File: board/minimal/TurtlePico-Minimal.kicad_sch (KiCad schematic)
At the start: 25 parts, among them J1 USB_C_Receptacle_USB2.0_14P, Q1 PMOS, Q2 PMOS, SW1 SW_Push, U1 RP2040, U2 STUSB4500QTR, U3 AP63203WU

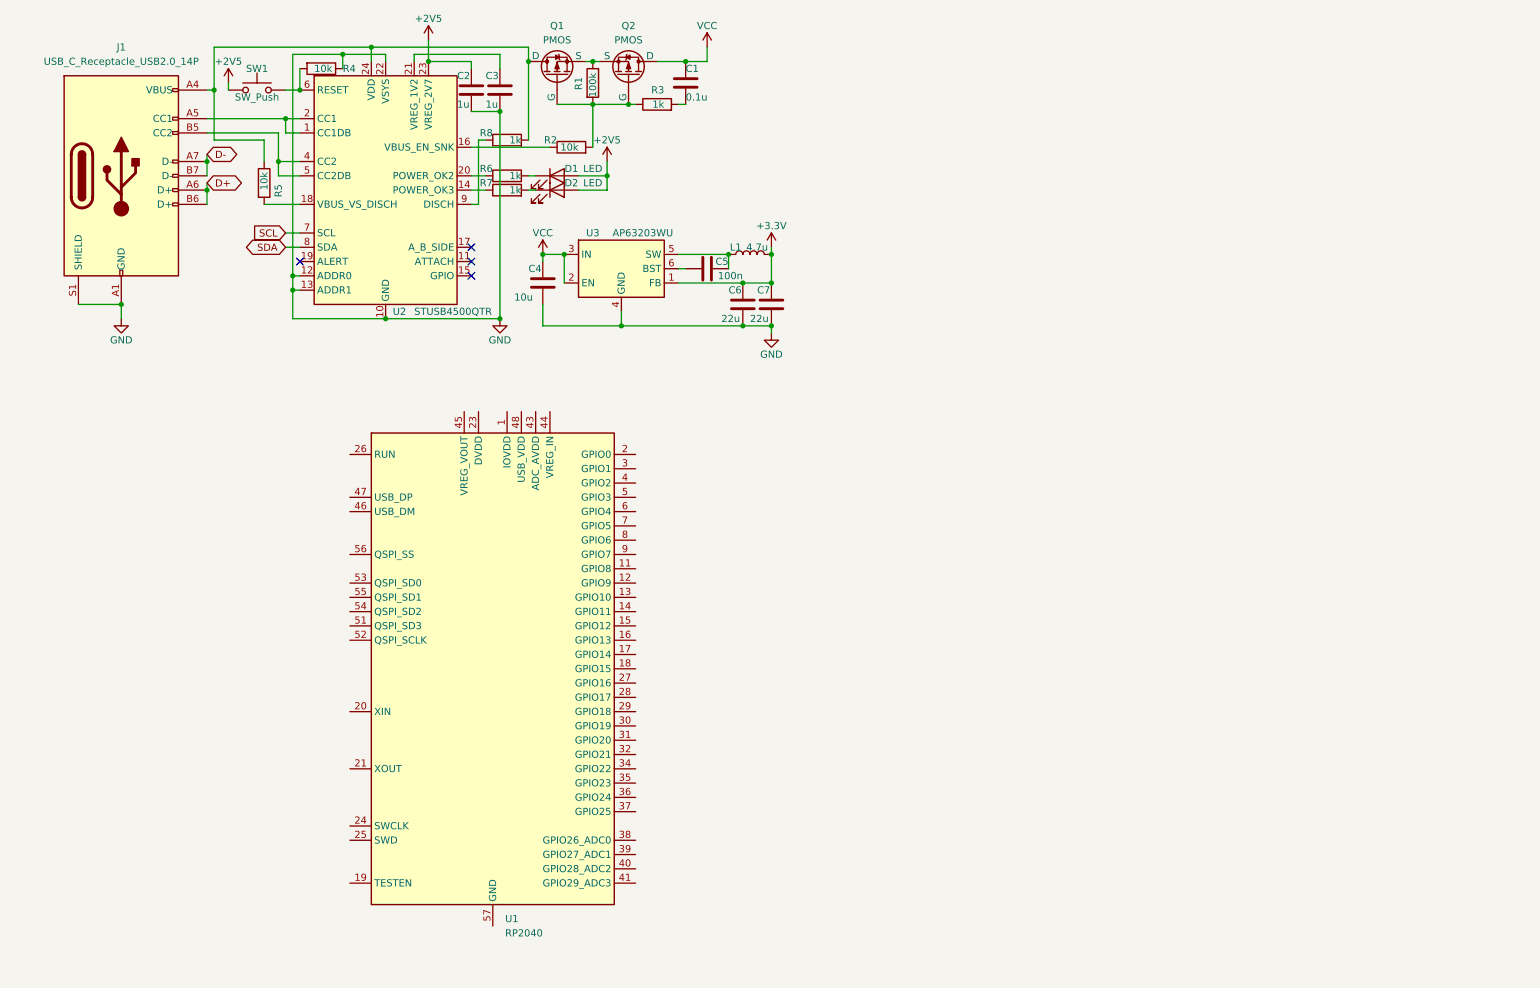
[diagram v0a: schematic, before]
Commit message: update minimal model
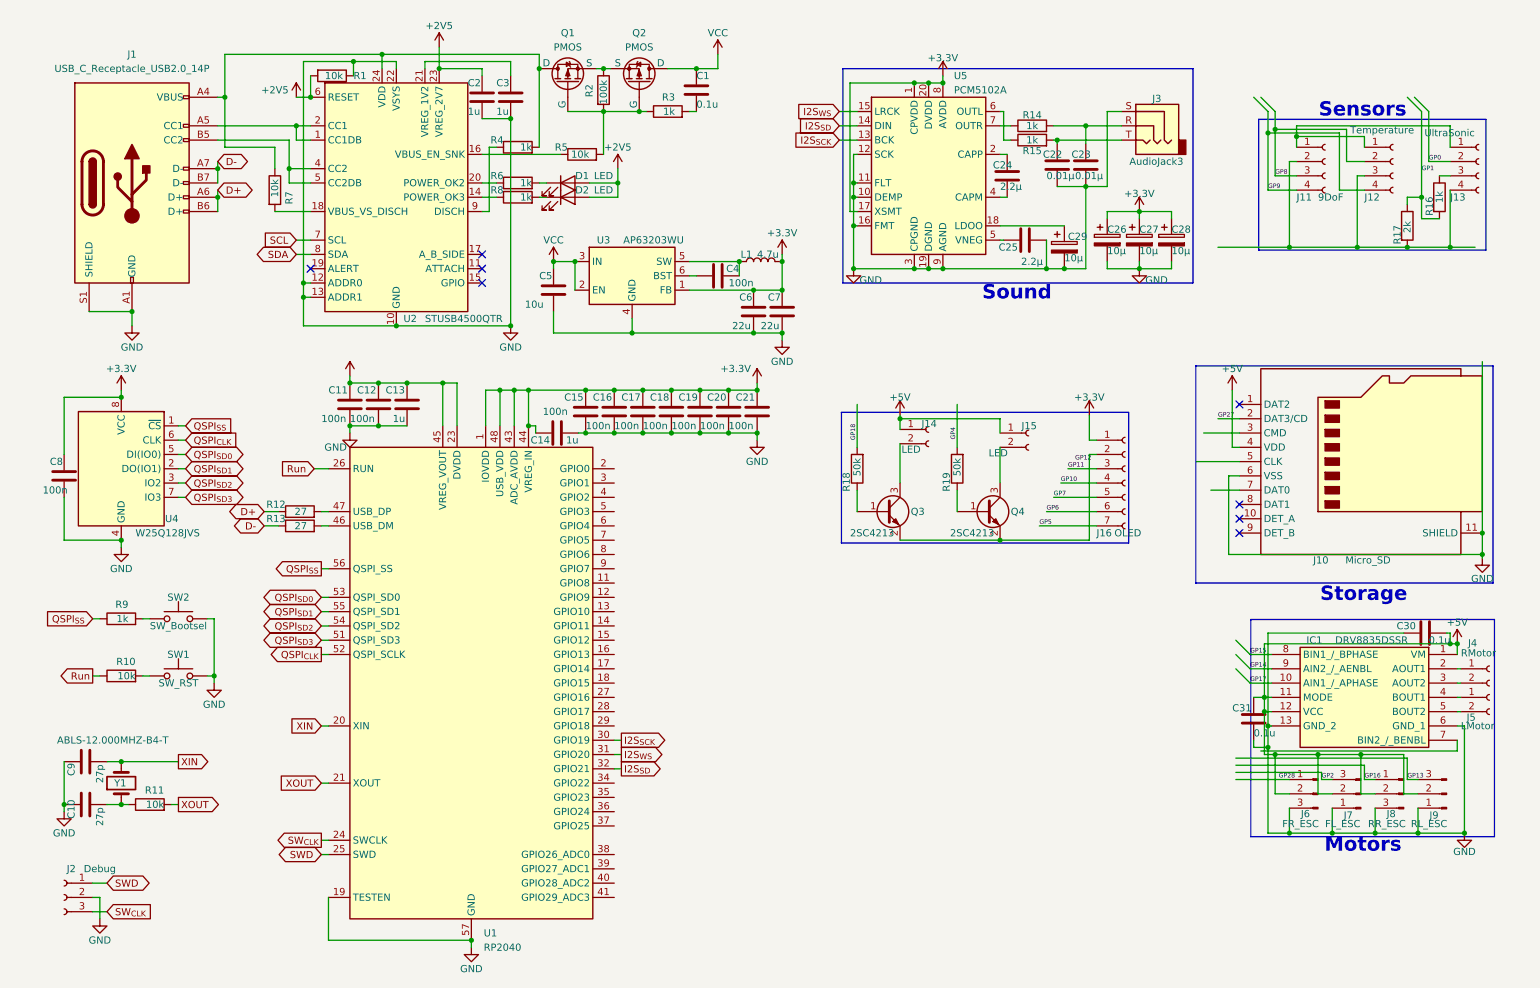
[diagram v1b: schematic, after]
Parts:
- added C10, C9: 27p, symbol Device:C
- added C11, C12, C15, C16, C17, C18, C19, C20, C21, C8: 100n, symbol Device:C
- added C13, C14: 1u, symbol Device:C
- added C22, C23: 0.01µ, Capacitor_SMD:C_0603_1608Metric, symbol Device:C
- added C24, C25: 2.2µ, Capacitor_SMD:C_0603_1608Metric, symbol Device:C
- added C26, C27, C28, C29: 10µ, Capacitor_SMD:CP_Elec_4x5.4, symbol Device:C_Polarized
- added C30, C31: 0.1u, Capacitor_SMD:C_0603_1608Metric, symbol Device:C
- added IC1: DRV8835DSSR, DRV8835DSSR, symbol DRV8835DSSR:DRV8835DSSR
- added J10: Micro_SD, Connector_Card:microSD_HC_Hirose_DM3AT-SF-PEJM5, symbol Connector:Micro_SD_Card_Det_Hirose_DM3AT
- added J11: 9DoF, Connector_JST:JST_XH_S4B-XH-A_1x04_P2.50mm_Horizontal, symbol Connector:Conn_01x04_Socket
- added J12: Temperature, Connector_PinSocket_2.54mm:PinSocket_1x04_P2.54mm_Vertical, symbol Connector:Conn_01x04_Socket
- added J13: UltraSonic, Connector_PinSocket_2.54mm:PinSocket_1x04_P2.54mm_Vertical, symbol Connector:Conn_01x04_Socket
- added J14, J15: LED, Connector_PinSocket_2.54mm:PinSocket_1x02_P2.54mm_Vertical, symbol Connector:Conn_01x02_Socket
- added J16: OLED, Connector_JST:JST_XH_S7B-XH-A_1x07_P2.50mm_Horizontal, symbol Connector:Conn_01x07_Socket
- added J2: Debug, symbol Connector:Conn_01x03_Socket
- added J3: AudioJack3, STX-3000:STX3000, symbol Connector_Audio:AudioJack3
- added J4: RMotor, Connector_PinSocket_2.54mm:PinSocket_1x02_P2.54mm_Vertical, symbol Connector:Conn_01x02_Socket
- added J5: LMotor, Connector_PinSocket_2.54mm:PinSocket_1x02_P2.54mm_Vertical, symbol Connector:Conn_01x02_Socket
- added J6: FR_ESC, Connector_PinHeader_2.54mm:PinHeader_1x03_P2.54mm_Horizontal, symbol Connector:Conn_01x03_Pin
- added J7: FL_ESC, Connector_PinHeader_2.54mm:PinHeader_1x03_P2.54mm_Horizontal, symbol Connector:Conn_01x03_Pin
- added J8: RR_ESC, Connector_PinHeader_2.54mm:PinHeader_1x03_P2.54mm_Horizontal, symbol Connector:Conn_01x03_Pin
- added J9: RL_ESC, Connector_PinHeader_2.54mm:PinHeader_1x03_P2.54mm_Horizontal, symbol Connector:Conn_01x03_Pin
- added Q3, Q4: 2SC4213, Package_TO_SOT_SMD:SOT-323_SC-70, symbol Transistor_BJT:2SC4213
- added R10, R11: 10k, symbol Device:R
- added R12, R13: 27, symbol Device:R
- added R14, R15, R16: 1k, Resistor_SMD:R_0603_1608Metric, symbol Device:R
- added R17: 2k, Resistor_SMD:R_0603_1608Metric, symbol Device:R
- added R18, R19: 50k, Resistor_SMD:R_0603_1608Metric, symbol Device:R
- added R9: 1k, symbol Device:R
- added SW2: SW_Bootsel, symbol Switch:SW_Push
- added U4: W25Q128JVS, Package_SO:SOIC-8_5.23x5.23mm_P1.27mm, symbol Memory_Flash:W25Q128JVS
- added U5: PCM5102A, Package_SO:TSSOP-20_4.4x6.5mm_P0.65mm, symbol Audio:PCM5102A
- added Y1: ABLS-12.000MHZ-B4-T, symbol Device:Crystal
- C4: value 10u -> 100n
- C5: value 100n -> 10u
- R1: value 100k -> 10k
- R2: value 10k -> 100k
- R4: value 10k -> 1k
- R7: value 1k -> 10k
- SW1: value SW_Push -> SW_RST
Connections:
- net +2V5: now also R1.2, U2.6 (RESET); no longer SW1.1
- net +3.3V: now also U1.1 (IOVDD), U1.10 (IOVDD), U1.22 (IOVDD), U1.33 (IOVDD), U1.42 (IOVDD), U1.43 (ADC_AVDD), U1.44 (VREG_IN), U1.48 (USB_VDD), U1.49 (IOVDD), C14.1, C15.1, C16.1, C17.1, C18.1, C19.1, C20.1, C21.1, C26.1, C27.1, C28.1, C8.1, J16.1 (Pin_1), U4.8 (VCC), U5.1 (CPVDD), U5.17 (XSMT), U5.20 (DVDD), U5.8 (AVDD)
- net D+: now also R12.1
- net D-: now also R13.1
- net GND: now also C5.2, R1.1, SW1.2, U1.19 (TESTEN), U1.57 (GND), C10.1, C11.2, C12.2, C13.2, C14.2, C15.2, C16.2, C17.2, C18.2, C19.2, C20.2, C21.2, C22.2, C23.2, C25.2, C26.2, C27.2, C28.2, C29.2, C30.2, C31.2, C8.2, C9.1, IC1.13 (GND_2), IC1.6 (GND_1), J10.11 (SHIELD), J10.6 (VSS), J2.2 (Pin_2), J3.S, J6.3 (Pin_3), J7.1 (Pin_1), J8.3 (Pin_3), J9.1 (Pin_1), SW2.2, U4.4 (GND), U5.10 (DEMP), U5.11 (FLT), U5.12 (SCK), U5.16 (FMT), U5.19 (DGND), U5.3 (CPGND), U5.9 (AGND); no longer C4.2, R4.1
- net VCC: now also C5.1; no longer C4.1
- net XIN: now reaches U1.20 (XIN)
- net XIN: now also C9.2, Y1.2
- net XOUT: now reaches U1.21 (XOUT)
- net XOUT: now also R11.2
- net +1V1: now reaches U1.23 (DVDD), U1.50 (DVDD)
- net +1V1: now also U1.45 (VREG_VOUT), C11.1, C12.1, C13.1
- net SW_{CLK}: now reaches U1.24 (SWCLK)
- net SW_{CLK}: now also J2.3 (Pin_3)
- net SWD: now reaches U1.25 (SWD)
- net SWD: now also J2.1 (Pin_1)
- net Run: now reaches U1.26 (RUN)
- net Run: now also R10.1
- net I2S_{SCK}: now reaches U1.30 (GPIO19)
- net I2S_{SCK}: now also U5.13 (BCK)
- net I2S_{WS}: now reaches U1.31 (GPIO20)
- net I2S_{WS}: now also U5.15 (LRCK)
- net I2S_{SD}: now reaches U1.32 (GPIO21)
- net I2S_{SD}: now also U5.14 (DIN)
- net at U1.46 (USB_DM): now also R13.2
- net at U1.47 (USB_DP): now also R12.2
- net QSPI_{SD3}: now reaches U1.51 (QSPI_SD3)
- net QSPI_{SD3}: now also U4.7 (IO3)
- net QSPI_{CLK}: now reaches U1.52 (QSPI_SCLK)
- net QSPI_{CLK}: now also U4.6 (CLK)
- net QSPI_{SD0}: now reaches U1.53 (QSPI_SD0)
- net QSPI_{SD0}: now also U4.5 (DI(IO0))
- net QSPI_{SD2}: now reaches U1.54 (QSPI_SD2)
- net QSPI_{SD2}: now also U4.3 (IO2)
- net QSPI_{SD1}: now reaches U1.55 (QSPI_SD1)
- net QSPI_{SD1}: now also U4.2 (DO(IO1))
- net QSPI_{SS}: now reaches U1.56 (QSPI_SS)
- net QSPI_{SS}: now also R9.1, U4.1 (~{CS})
- net at R2.1: now also Q1.3 (S), Q2.3 (S); no longer U2.16 (VBUS_EN_SNK)
- net at Q1.2 (G), Q2.2 (G), R2.2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: now also R5.2; no longer R1.2
- net at L1.1, U3.5 (SW): now also C4.2; no longer C5.2
- net at J1.A4 (VBUS), J1.A9 (VBUS), J1.B4 (VBUS)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: now also R4.2, R7.1; no longer R5.1, R8.2
- net at U3.6 (BST): now also C4.1; no longer C5.1
- net at U2.18 (VBUS_VS_DISCH): now also R7.2; no longer R5.2
- net at R8.1: now also U2.14 (POWER_OK3); no longer U2.9 (DISCH)
- net at D2.1 (K): now also R8.2; no longer R7.2
- new net: R14.1, U5.7 (OUTR)
- new net: C23.1, J3.R, R14.2
- new net: J11.1 (Pin_1), J12.1 (Pin_1), J13.1 (Pin_1)
- new net: J11.2 (Pin_2), J12.3 (Pin_3), J13.4 (Pin_4), R17.2
- new net: C22.1, J3.T, R15.2
- new net: Q4.1 (B), R19.1
- new net: C10.2, R11.1, Y1.1
- new net: R15.1, U5.6 (OUTL)
- new net: J13.3 (Pin_3), R16.1
- new net: R5.1, U2.16 (VBUS_EN_SNK)
- new net: J16.2 (Pin_2), Q3.2 (E), Q4.2 (E)
- new net: C25.1, U5.5 (VNEG)
- new net: R9.2, SW2.1
- new net: J14.2 (Pin_2), Q3.3 (C)
- new net: IC1.4 (BOUT1), J5.1 (Pin_1)
- new net: IC1.5 (BOUT2), J5.2 (Pin_2)
- new net: Q3.1 (B), R18.1
- new net: J15.2 (Pin_2), Q4.3 (C)
- new net: C29.1, U5.18 (LDOO)
- new net: C24.1, U5.2 (CAPP)
- new net: C24.2, U5.4 (CAPM)
- new net: IC1.2 (AOUT1), J4.1 (Pin_1)
- new net: IC1.3 (AOUT2), J4.2 (Pin_2)
- new net: R4.1, U2.9 (DISCH)
- new net: R10.2, SW1.1
- new net +5V: C30.1, C31.1, IC1.1 (VM), IC1.11 (MODE), IC1.12 (VCC), J10.4 (VDD), J14.1 (Pin_1), J15.1 (Pin_1), J6.2 (Pin_2), J7.2 (Pin_2), J8.2 (Pin_2), J9.2 (Pin_2)
- new net GP0: J13.2 (Pin_2)
- new net GP1: R16.2, R17.1
- new net GP10: J16.4 (Pin_4)
- new net GP11: J16.3 (Pin_3)
- new net GP13: J9.3 (Pin_3)
- new net GP14: IC1.9 (AIN2_/_AENBL)
- new net GP15: IC1.8 (BIN1_/_BPHASE)
- new net GP16: J8.1 (Pin_1)
- new net GP17: IC1.10 (AIN1_/_APHASE)
- new net GP18: R18.2
- new net GP2: J7.3 (Pin_3)
- new net GP27: J10.2 (DAT3/CD)
- new net GP28: J6.1 (Pin_1)
- new net GP4: R19.2
- new net GP5: J16.7 (Pin_7)
- new net GP6: J16.6 (Pin_6)
- new net GP7: J16.5 (Pin_5)
- new net GP8: J11.3 (Pin_3), J12.2 (Pin_2)
- new net GP9: J11.4 (Pin_4), J12.4 (Pin_4)
- no-connect marks 4 -> 8
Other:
- note added: "Motors"
- note added: "Sensors"
- note added: "Sound"
- note added: "Storage"
- moved on the sheet: U1

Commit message: update schematics
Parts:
- added D3, D4: LED, symbol Device:LED
- added Q5, Q6: PMOS, symbol Simulation_SPICE:PMOS
- added R13, R14: 1k, Resistor_SMD:R_0603_1608Metric, symbol Device:R
- added R22: 10k, Resistor_SMD:R_0603_1608Metric, symbol Device:R
- added SW3: SW_{R}, symbol Switch:SW_Push
- added SW4: SW_{L}, symbol Switch:SW_Push
- R11: renamed from R18; value 50k -> 5k
- R12: renamed from R19; value 50k -> 5k
- renumbered C13 to C10, C15 to C11, C16 to C12, C17 to C13, C18 to C14, C19 to C15, C20 to C16, C21 to C17, C14 to C18, C8 to C19, C30 to C20, C31 to C21, C9 to C30, C10 to C31, C11 to C8, C12 to C9, J11 to J1, J5 to J10, J3 to J11, J6 to J12, J7 to J13, J8 to J14, J9 to J15, J2 to J16, J12 to J2, J13 to J3, J1 to J4, J14 to J5, J15 to J6, J16 to J7, J10 to J8, J4 to J9, R17 to R10, R12 to R15, R13 to R16, R9 to R17, R14 to R18, R15 to R19, R10 to R20, R11 to R21, R16 to R9, SW2 to SW1, SW1 to SW2, U3 to U1, U4 to U3, U5 to U4, U1 to U5
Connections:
- net GP0 is gone; now on net Tx/TRIG: J3.2 (Pin_2)
- net GP10 is gone; now on net SPI_{SCK}: J7.4 (Pin_4)
- net GP11 is gone; now on net SPI_{MOSI}: J7.3 (Pin_3)
- net GP13 is gone; now on net ESC_{RL}: J15.3 (Pin_3)
- net GP14 is gone; now on net MOTOR_A_{EN}: IC1.9 (AIN2_/_AENBL)
- net GP15 is gone; now on net MOTOR_B_{IN}: IC1.8 (BIN1_/_BPHASE)
- net GP16 is gone; now on net ESC_{RR}: J14.1 (Pin_1)
- net GP17 is gone; now on net MOTOR_A_{IN}: IC1.10 (AIN1_/_APHASE)
- net GP18 is gone; now on net LED_{R}: R11.2
- net GP2 is gone; now on net ESC_{FL}: J13.3 (Pin_3)
- net GP27 is gone; now on net SD_{CS}: J8.2 (DAT3/CD)
- net GP28 is gone; now on net ESC_{FR}: J12.1 (Pin_1)
- net GP4 is gone; now on net LED_{L}: R12.2
- net GP5 is gone; now on net OLED_{RST}: J7.7 (Pin_7)
- net GP6 is gone; now on net OLED_{DC}: J7.6 (Pin_6)
- net GP7 is gone; now on net OLED_{CS}: J7.5 (Pin_5)
- net GP8 is gone; now on net SDA: J1.3 (Pin_3), J2.2 (Pin_2)
- net GP9 is gone; now on net SCL: J1.4 (Pin_4), J2.4 (Pin_4)
- net +3.3V: now also C21.1, IC1.11 (MODE), IC1.12 (VCC), J1.1 (Pin_1), J2.1 (Pin_1), J3.1 (Pin_1), J5.1 (Pin_1), J6.1 (Pin_1), J8.4 (VDD), Q5.1 (D), SW3.1, SW4.1
- net GND: now also J1.2 (Pin_2), J2.3 (Pin_3), J3.4 (Pin_4), J7.2 (Pin_2), Q3.2 (E), Q4.2 (E), R10.1, R13.1, R14.1, R22.1
- net SCL: now also U5.12 (GPIO9)
- net SDA: now also U5.11 (GPIO8)
- net VCC: now also C20.1, IC1.1 (VM)
- net at C23.1, J11.R, R18.2: now also C22.1, J11.T, R19.2
- net SPI_{SCK}: now reaches U5.13 (GPIO10)
- net SPI_{SCK}: now also J8.5 (CLK)
- net SPI_{MOSI}: now reaches U5.14 (GPIO11)
- net SPI_{MOSI}: now also J8.3 (CMD)
- net SPI_{MISO}: now reaches U5.15 (GPIO12)
- net SPI_{MISO}: now also J8.7 (DAT0)
- net ESC_{RL}: now reaches U5.16 (GPIO13)
- net MOTOR_A_{EN}: now reaches U5.17 (GPIO14)
- net MOTOR_B_{IN}: now reaches U5.18 (GPIO15)
- net Rx/Echo: now reaches U5.2 (GPIO0)
- net Rx/Echo: now also R10.2, R9.2
- net ESC_{RR}: now reaches U5.27 (GPIO16)
- net MOTOR_A_{IN}: now reaches U5.28 (GPIO17)
- net LED_{R}: now reaches U5.29 (GPIO18)
- net LED_{R}: now also D4.2 (A)
- net Tx/TRIG: now reaches U5.3 (GPIO1)
- net SW_{R}: now reaches U5.34 (GPIO22)
- net SW_{R}: now also SW3.2
- net MOTOR_B_{EN}: now reaches U5.35 (GPIO23)
- net MOTOR_B_{EN}: now also IC1.7 (BIN2_/_BENBL)
- net SD_{CS}: now reaches U5.39 (GPIO27_ADC1)
- net ESC_{FL}: now reaches U5.4 (GPIO2)
- net ESC_{FR}: now reaches U5.40 (GPIO28_ADC2)
- net SW_{L}: now reaches U5.5 (GPIO3)
- net SW_{L}: now also SW4.2
- net LED_{L}: now reaches U5.6 (GPIO4)
- net LED_{L}: now also D3.2 (A)
- net OLED_{RST}: now reaches U5.7 (GPIO5)
- net OLED_{DC}: now reaches U5.8 (GPIO6)
- net OLED_{CS}: now reaches U5.9 (GPIO7)
- net VBUS: now reaches J4.A4 (VBUS), J4.A9 (VBUS), J4.B4 (VBUS), J4.B9 (VBUS), Q1.1 (D), R4.2, R7.1, U2.24 (VDD)
- net +2V5 renamed +2V8
- removed net +5V: C20.1, C21.1, IC1.1 (VM), IC1.11 (MODE), IC1.12 (VCC), J12.2 (Pin_2), J13.2 (Pin_2), J14.2 (Pin_2), J15.2 (Pin_2), J5.1 (Pin_1), J6.1 (Pin_1), J8.4 (VDD)
- removed net GP1: R10.1, R9.2
- new net: J12.2 (Pin_2), J13.2 (Pin_2), J14.2 (Pin_2), J15.2 (Pin_2), Q5.2 (G), Q6.1 (D), Q6.2 (G), R22.2
- new net: Q5.3 (S), Q6.3 (S)
- new net: D3.1 (K), R13.2
- new net: D4.1 (K), R14.2
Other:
- note removed: "Motors"
- note removed: "Sensors"
- note removed: "Sound"
- note removed: "Storage"
- moved on the sheet: C1, C19, C2, C20, C21, C22, C23, C24, C25, C26, C27, C28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

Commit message: update schematics
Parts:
- removed C1: 0.1u, symbol Device:C
- removed C10, C18, C2, C3: 1u, symbol Device:C
- removed C11, C12, C13, C14, C15, C16, C17, C19, C4, C8, C9: 100n, symbol Device:C
- removed C20, C21: 0.1u, Capacitor_SMD:C_0603_1608Metric, symbol Device:C
- removed C22, C23: 0.01µ, Capacitor_SMD:C_0603_1608Metric, symbol Device:C
- removed C24, C25: 2.2µ, Capacitor_SMD:C_0603_1608Metric, symbol Device:C
- removed C26, C27, C28, C29: 10µ, Capacitor_SMD:CP_Elec_4x5.4, symbol Device:C_Polarized
- removed C30, C31: 27p, symbol Device:C
- removed C5: 10u, symbol Device:C
- removed C6, C7: 22u, symbol Device:C
- removed D1, D2, D3, D4: LED, symbol Device:LED
- removed IC1: DRV8835DSSR, DRV8835DSSR, symbol DRV8835DSSR:DRV8835DSSR
- removed J1: 9DoF, Connector_JST:JST_XH_S4B-XH-A_1x04_P2.50mm_Horizontal, symbol Connector:Conn_01x04_Socket
- removed J10: LMotor, Connector_PinSocket_2.54mm:PinSocket_1x02_P2.54mm_Vertical, symbol Connector:Conn_01x02_Socket
- removed J11: AudioJack3, STX-3000:STX3000, symbol Connector_Audio:AudioJack3
- removed J12: FR_ESC, Connector_PinHeader_2.54mm:PinHeader_1x03_P2.54mm_Horizontal, symbol Connector:Conn_01x03_Pin
- removed J13: FL_ESC, Connector_PinHeader_2.54mm:PinHeader_1x03_P2.54mm_Horizontal, symbol Connector:Conn_01x03_Pin
- removed J14: RR_ESC, Connector_PinHeader_2.54mm:PinHeader_1x03_P2.54mm_Horizontal, symbol Connector:Conn_01x03_Pin
- removed J15: RL_ESC, Connector_PinHeader_2.54mm:PinHeader_1x03_P2.54mm_Horizontal, symbol Connector:Conn_01x03_Pin
- removed J16: Debug, symbol Connector:Conn_01x03_Socket
- removed J2: Temperature, Connector_PinSocket_2.54mm:PinSocket_1x04_P2.54mm_Vertical, symbol Connector:Conn_01x04_Socket
- removed J3: UltraSonic, Connector_PinSocket_2.54mm:PinSocket_1x04_P2.54mm_Vertical, symbol Connector:Conn_01x04_Socket
- removed J4: USB_C_Receptacle_USB2.0_14P, symbol Connector:USB_C_Receptacle_USB2.0_14P
- removed J5, J6: LED, Connector_PinSocket_2.54mm:PinSocket_1x02_P2.54mm_Vertical, symbol Connector:Conn_01x02_Socket
- removed J7: OLED, Connector_JST:JST_XH_S7B-XH-A_1x07_P2.50mm_Horizontal, symbol Connector:Conn_01x07_Socket
- removed J8: Micro_SD, Connector_Card:microSD_HC_Hirose_DM3AT-SF-PEJM5, symbol Connector:Micro_SD_Card_Det_Hirose_DM3AT
- removed J9: RMotor, Connector_PinSocket_2.54mm:PinSocket_1x02_P2.54mm_Vertical, symbol Connector:Conn_01x02_Socket
- removed L1: 4.7u, symbol Device:L
- removed Q1, Q2, Q5, Q6: PMOS, symbol Simulation_SPICE:PMOS
- removed Q3, Q4: 2SC4213, Package_TO_SOT_SMD:SOT-323_SC-70, symbol Transistor_BJT:2SC4213
- removed R1, R20, R21, R5, R7: 10k, symbol Device:R
- removed R10: 2k, Resistor_SMD:R_0603_1608Metric, symbol Device:R
- removed R11, R12: 5k, Resistor_SMD:R_0603_1608Metric, symbol Device:R
- removed R13, R14, R18, R19, R9: 1k, Resistor_SMD:R_0603_1608Metric, symbol Device:R
- removed R15, R16: 27, symbol Device:R
- removed R17, R3, R4, R6, R8: 1k, symbol Device:R
- removed R2: 100k, symbol Device:R
- removed R22: 10k, Resistor_SMD:R_0603_1608Metric, symbol Device:R
- removed SW1: SW_Bootsel, symbol Switch:SW_Push
- removed SW2: SW_RST, symbol Switch:SW_Push
- removed SW3: SW_{R}, symbol Switch:SW_Push
- removed SW4: SW_{L}, symbol Switch:SW_Push
- removed U1: AP63203WU, Package_TO_SOT_SMD:TSOT-23-6, symbol Regulator_Switching:AP63203WU
- removed U2: STUSB4500QTR, Package_DFN_QFN:QFN-24-1EP_4x4mm_P0.5mm_EP2.7x2.7mm, symbol Interface_USB:STUSB4500QTR
- removed U3: W25Q128JVS, Package_SO:SOIC-8_5.23x5.23mm_P1.27mm, symbol Memory_Flash:W25Q128JVS
- removed U4: PCM5102A, Package_SO:TSSOP-20_4.4x6.5mm_P0.65mm, symbol Audio:PCM5102A
- removed U5: RP2040, Package_DFN_QFN:QFN-56-1EP_7x7mm_P0.4mm_EP3.2x3.2mm, symbol MCU_RaspberryPi:RP2040
- removed Y1: ABLS-12.000MHZ-B4-T, symbol Device:Crystal
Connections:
- no-connect marks 8 -> 0
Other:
- added sheet Audio (Audio.kicad_sch)
- added sheet Connector (Connector.kicad_sch)
- added sheet LED_Switch (LED_Switch.kicad_sch)
- added sheet Motor (Motor.kicad_sch)
- added sheet Power_USB (Power_USB.kicad_sch)
- added sheet RP2040 (RP2040.kicad_sch)
- added sheet Sensor (Sensor.kicad_sch)
- added sheet Storage (Storage.kicad_sch)
